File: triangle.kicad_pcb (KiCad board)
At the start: 2 copper layers, 80.6 x 72.4 mm, 55 parts, among them J1 Conn_01x02, SW1 SW_SPST

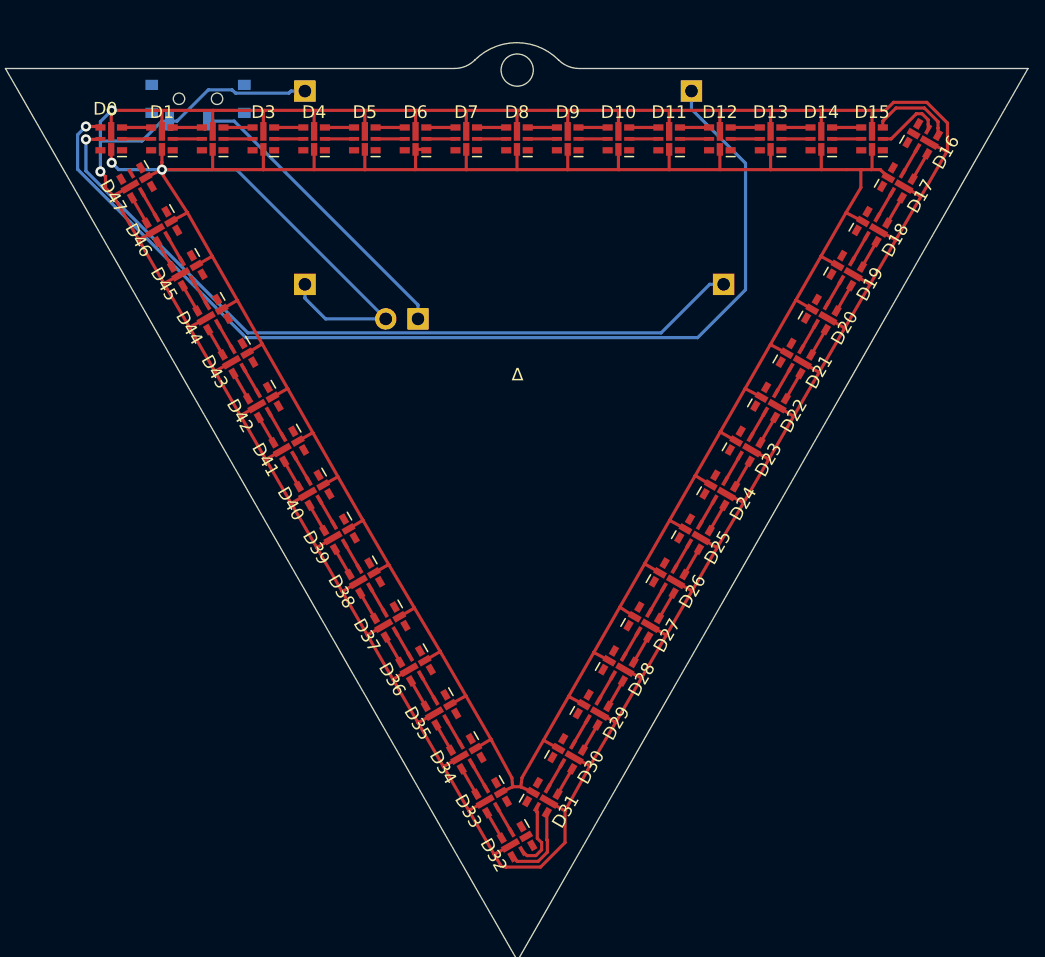
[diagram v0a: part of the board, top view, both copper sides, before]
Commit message: hide led numbers; scoot boards over to minimize overhang
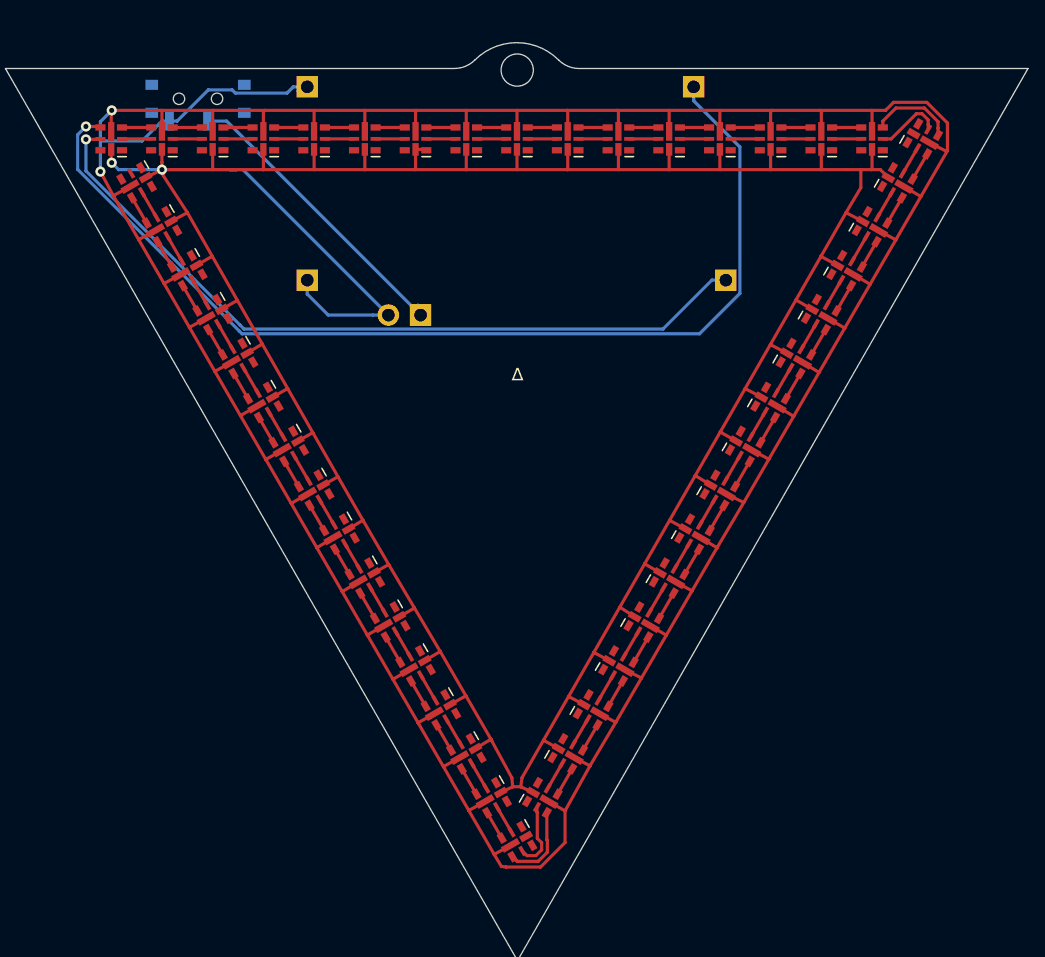
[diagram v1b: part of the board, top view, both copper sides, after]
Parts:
- moved DATA 0.38 mm to (95.9, 45.9)
- moved SCK 0.38 mm to (98.5, 61.1)
- moved +5V 0.38 mm to (65.5, 61.1)
- moved GND 0.38 mm to (65.5, 45.9)
- moved J1 0.37 mm to (74.4, 63.9)
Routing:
- net +5V: track 271.0 -> 271.6 mm
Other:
- board text removed: "D0"

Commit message: sign it
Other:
- board text added: "∆ by opal"
- board text removed: "∆"
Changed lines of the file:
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@@
   (general
     (thickness 1.6)
-    (drawings 18)
+    (drawings 21)
     (tracks 424)
     (zones 0)
@@
     )
   )
+  (gr_line (start 82.0166 69.02196) (end 83.2866 71.2216) (layer F.SilkS) (width 0.12))
+  (gr_line (start 80.7466 71.2216) (end 83.2866 71.2216) (layer F.SilkS) (width 0.12))
+  (gr_line (start 80.7466 71.2216) (end 82.0166 69.02196) (layer F.SilkS) (width 0.12))
+  (gr_text "∆ by opal" (at 88.4428 100.1014 60) (layer F.SilkS)
+    (effects (font (size 1.016 1.016) (thickness 0.1016)))
+  )
   (gr_line (start 82.042 114.808) (end 41.656 44.45) (layer Edge.Cuts) (width 0.05))
   (gr_line (start 86.90049 44.45) (end 122.301 44.45) (layer Edge.Cuts) (width 0.05))
@@
   (gr_arc (start 81.982045 47.082445) (end 78.680046 43.780446) (angle 90) (layer Edge.Cuts) (width 0.05))
   (gr_arc (start 77.0636 42.164) (end 77.0636 44.45) (angle -45) (layer Edge.Cuts) (width 0.05))
-  (gr_text ∆ (at 82.042 68.58) (layer F.SilkS)
-    (effects (font (size 1 1) (thickness 0.15)))
-  )
   (gr_line (start 99.7966 62.6237) (end 64.2366 62.6237) (layer B.SilkS) (width 0.12))
   (gr_line (start 64.2366 84.2137) (end 64.2366 62.6237) (layer B.SilkS) (width 0.12))
